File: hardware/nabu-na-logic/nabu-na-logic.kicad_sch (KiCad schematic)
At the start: 22 parts, among them J1 Conn_01x09_Pin, U1 74LS164, U12 74LS164, U13 74LS164, U14 74HC04, U15 74LS74, U2 74LS30, U20 74LS164, U21 74HC86, U22 74LS74, U23 74LS00, U24 74HC04, U26 74LS74, U3 74LS27, U4 74LS164

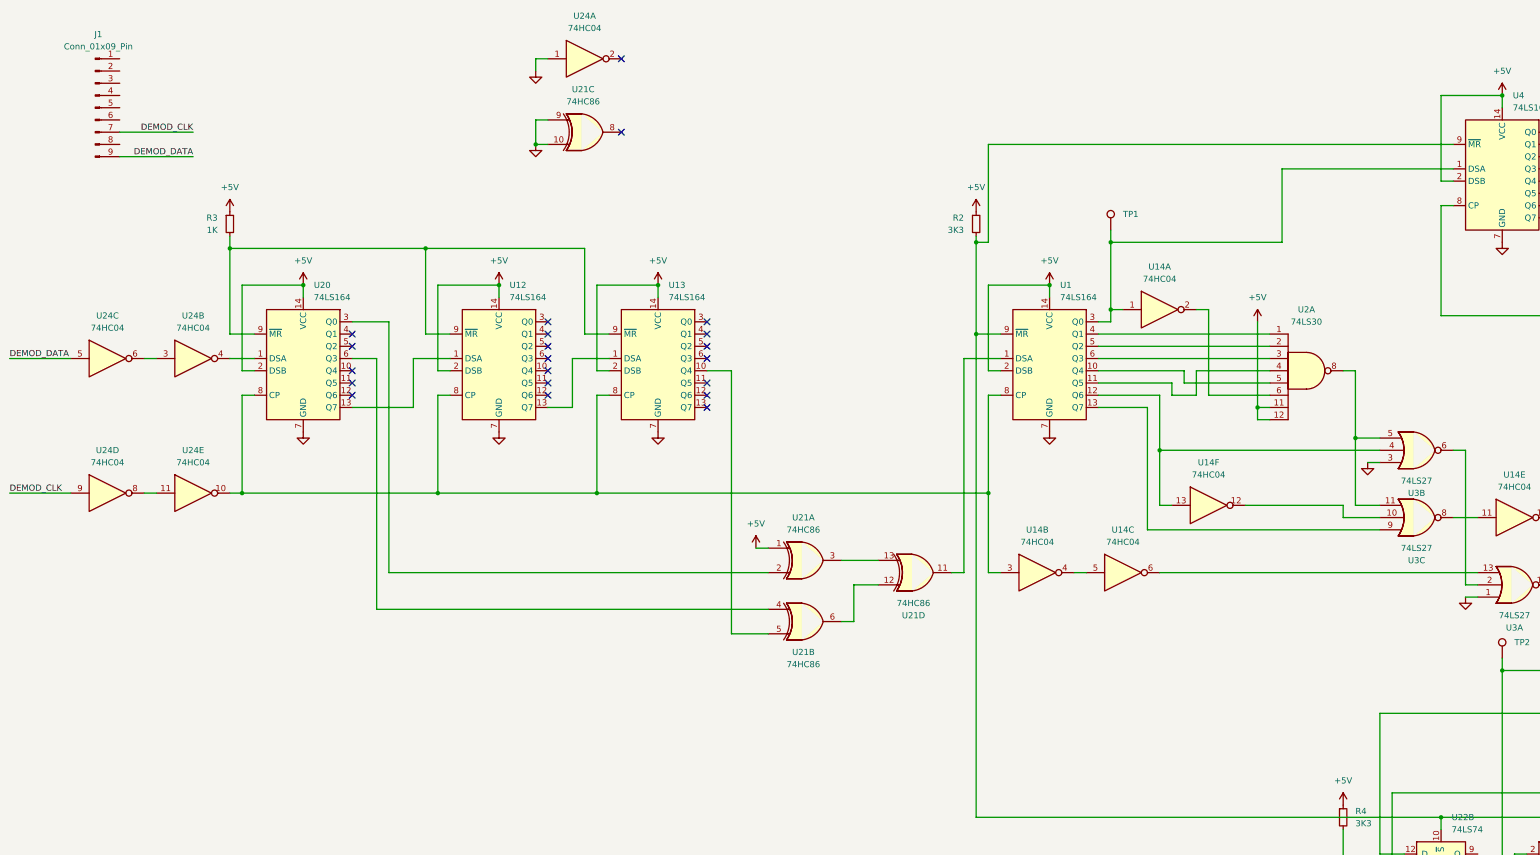
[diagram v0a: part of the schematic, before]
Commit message: Initial, partial work on processor and surroundings, move descrambler to separate sheet
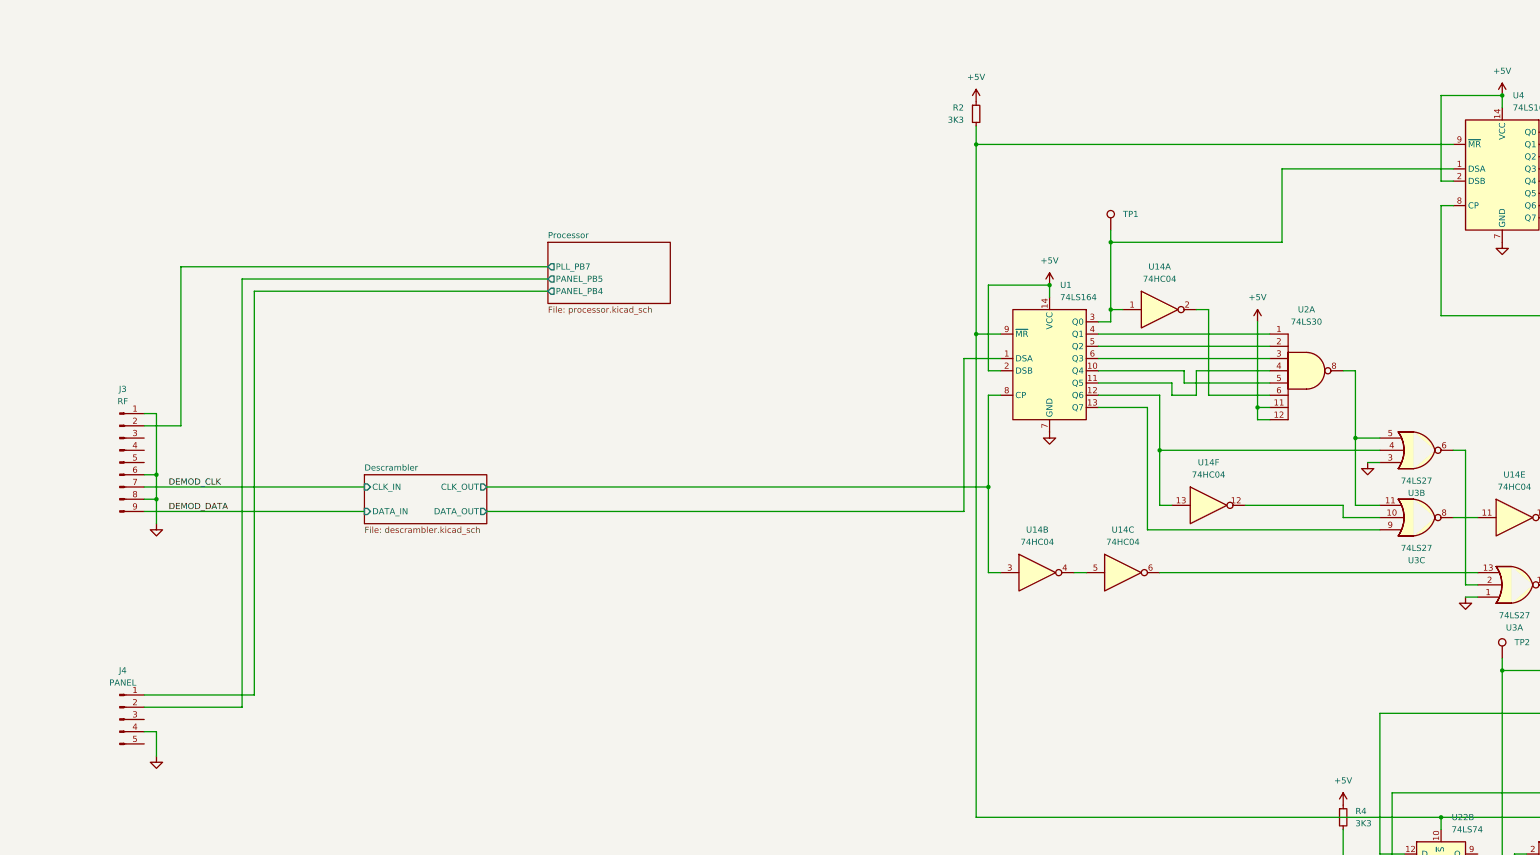
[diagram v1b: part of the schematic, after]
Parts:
- removed R3: 1K, symbol Device:R_Small
- removed U12, U13, U20: 74LS164, symbol 74xx:74HC164
- removed U21: 74HC86, symbol 74xx:74HC86
- removed unit 2 of U24
- removed unit 5 of U24
- removed unit 3 of U24
- removed unit 4 of U24
- removed unit 1 of U24
- added J4: PANEL, symbol Connector:Conn_01x05_Pin
- J3: renamed from J1; value Conn_01x09_Pin -> RF
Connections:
- net GND: now also J3.1 (Pin_1), J3.6 (Pin_6), J3.8 (Pin_8), J4.4 (Pin_4)
- net Descrambler/DATA_OUT: now reaches U1.1 (DSA)
- net Descrambler/CLK_OUT: now reaches U1.8 (CP), U14.3
- net Processor/PLL_PB7: now reaches J3.2 (Pin_2)
- new net Processor/PANEL_PB4: J4.1 (Pin_1)
- new net Processor/PANEL_PB5: J4.2 (Pin_2)
- no-connect marks 24 -> 3
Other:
- added sheet Descrambler (descrambler.kicad_sch)
- added sheet Processor (processor.kicad_sch)
- moved on the sheet: J3, R2

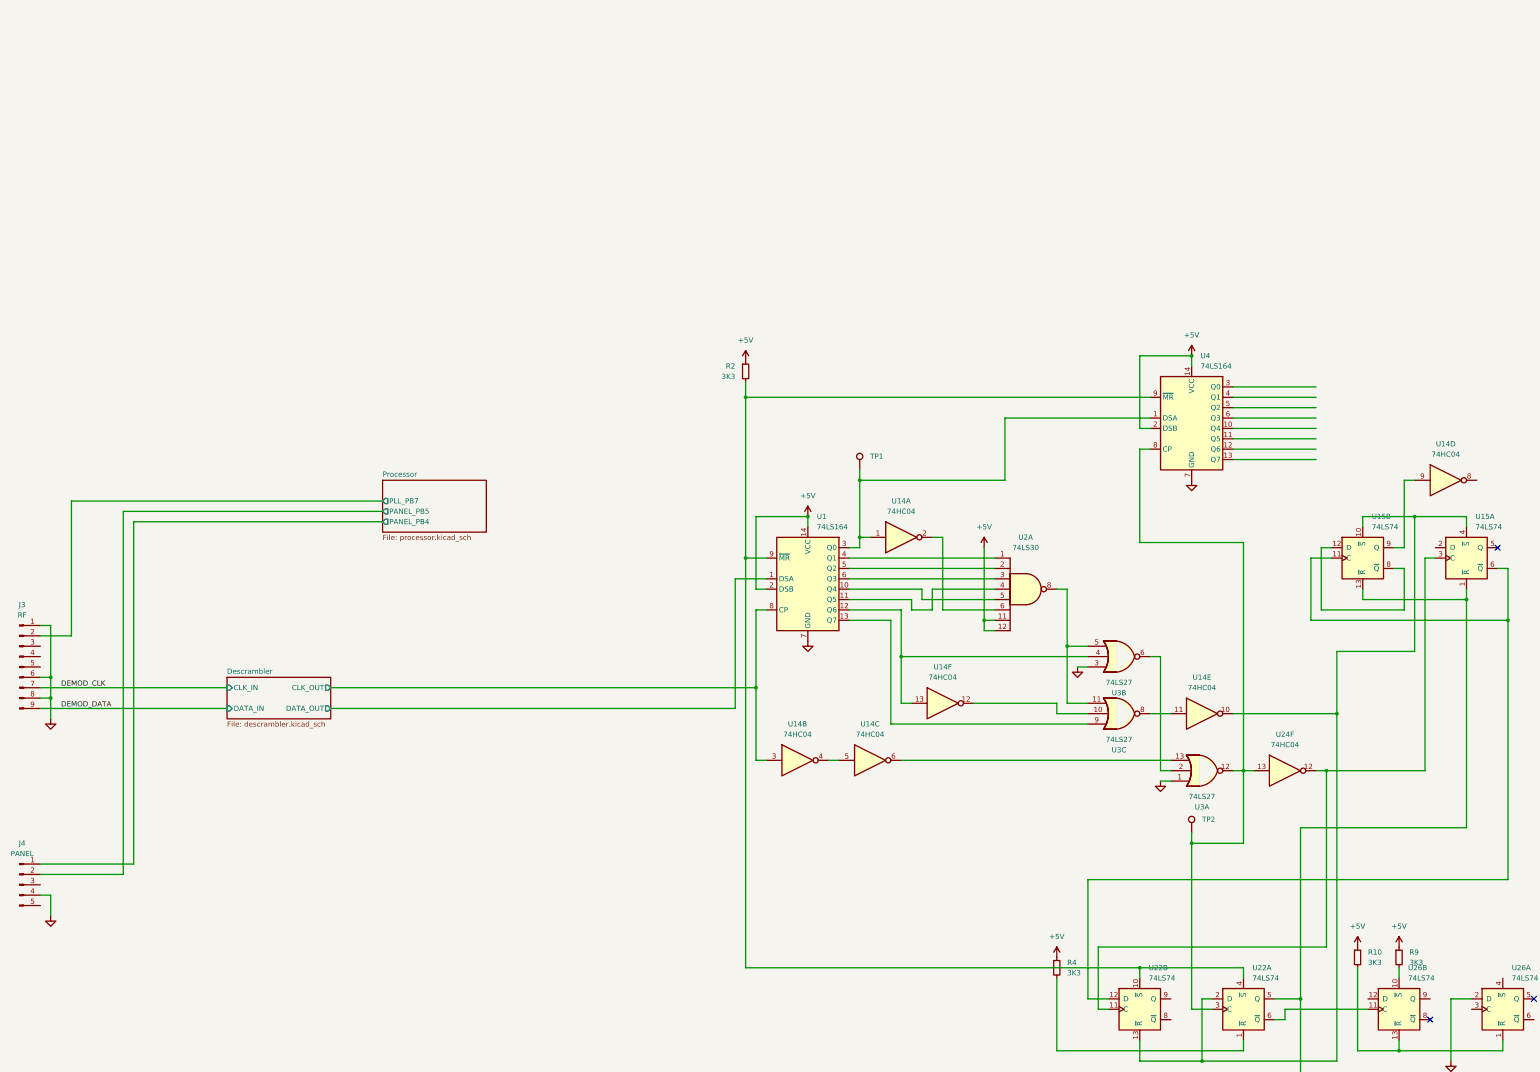
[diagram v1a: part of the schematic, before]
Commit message: Logic board schematic: Add PAL, assorted changes I've forgotten already.
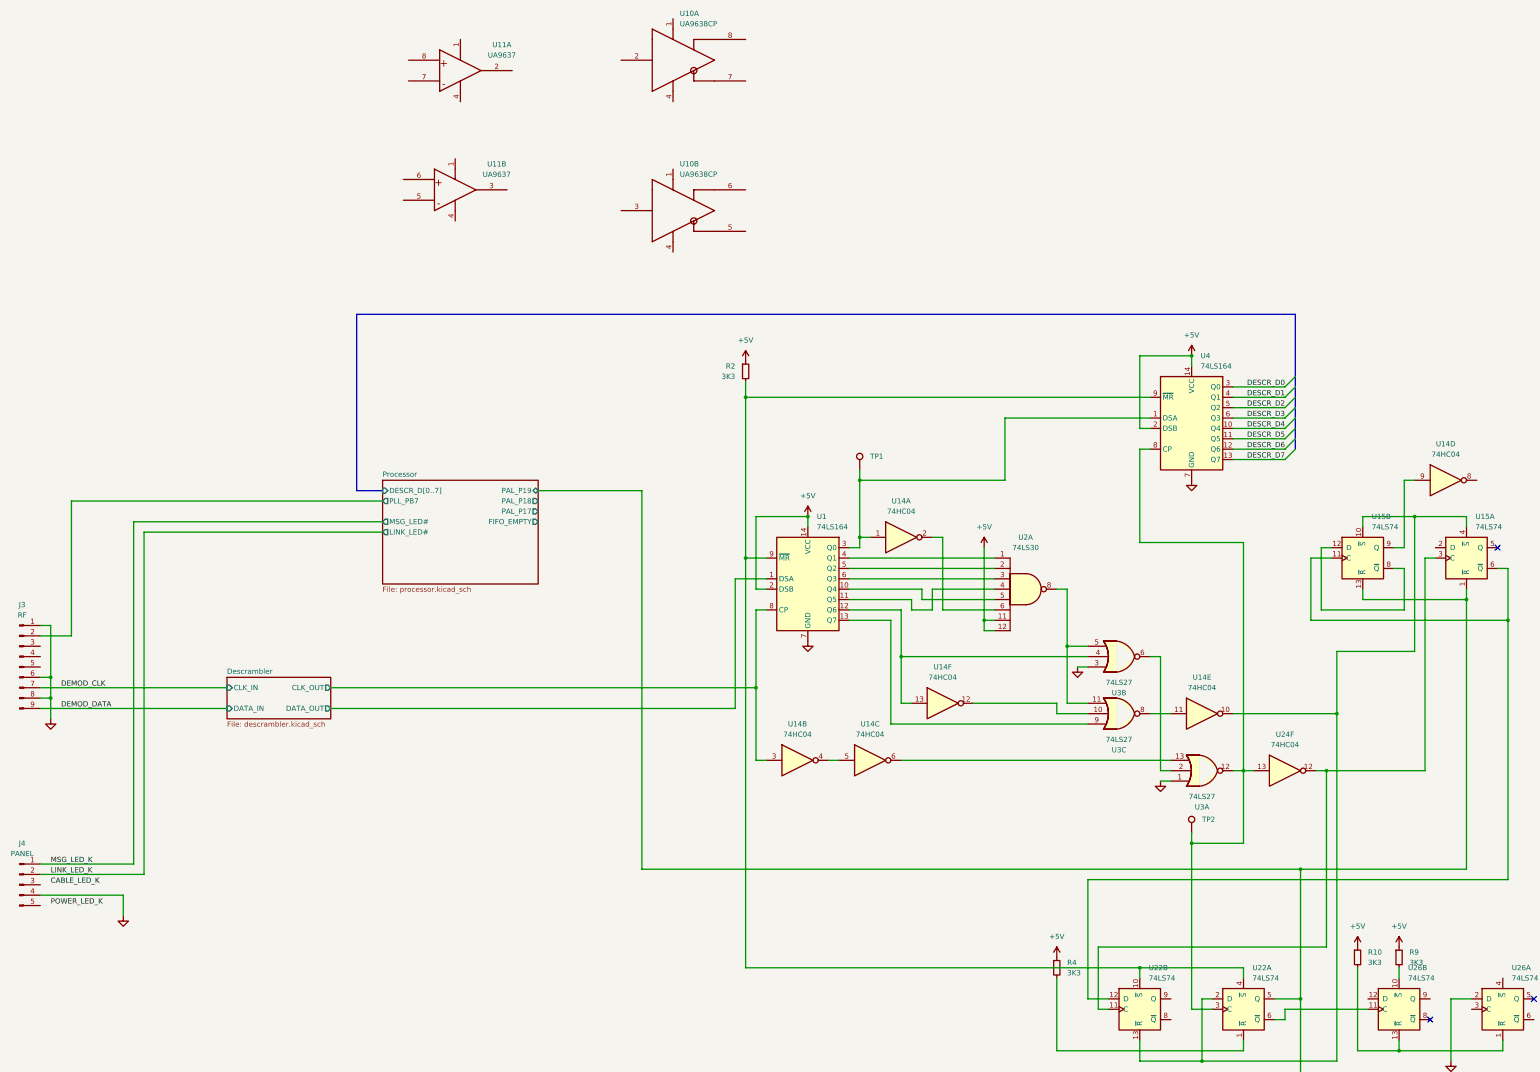
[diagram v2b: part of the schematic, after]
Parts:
- added U10: UA9638CP, Package_DIP:DIP-8_W7.62mm, symbol Interface_LineDriver:UA9638CP
- added U11: UA9637, Package_DIP:DIP-8_W7.62mm, symbol Interface_LineDriver:UA9637
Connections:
- net Processor/PAL_P19: now reaches U15.1 (~{R}), U15.13 (~{R}), U22.5 (Q), U23.2
- net DESCR_D4: now reaches U4.10 (Q4)
- net DESCR_D5: now reaches U4.11 (Q5)
- net DESCR_D6: now reaches U4.12 (Q6)
- net DESCR_D7: now reaches U4.13 (Q7)
- net DESCR_D0: now reaches U4.3 (Q0)
- net DESCR_D1: now reaches U4.4 (Q1)
- net DESCR_D2: now reaches U4.5 (Q2)
- net DESCR_D3: now reaches U4.6 (Q3)
- net Processor/PANEL_PB4 renamed MSG_LED_K
- net Processor/PANEL_PB5 renamed LINK_LED_K
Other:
- sheet Processor ports: added DESCR_D[0..7], FIFO_EMPTY, LINK_LED#, MSG_LED#, PAL_P17, PAL_P18, PAL_P19; removed PANEL_PB4, PANEL_PB5
